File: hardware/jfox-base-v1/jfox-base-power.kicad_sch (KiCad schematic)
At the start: 13 parts, among them J50 PWR 1 RH, J51 PWR 2 LH

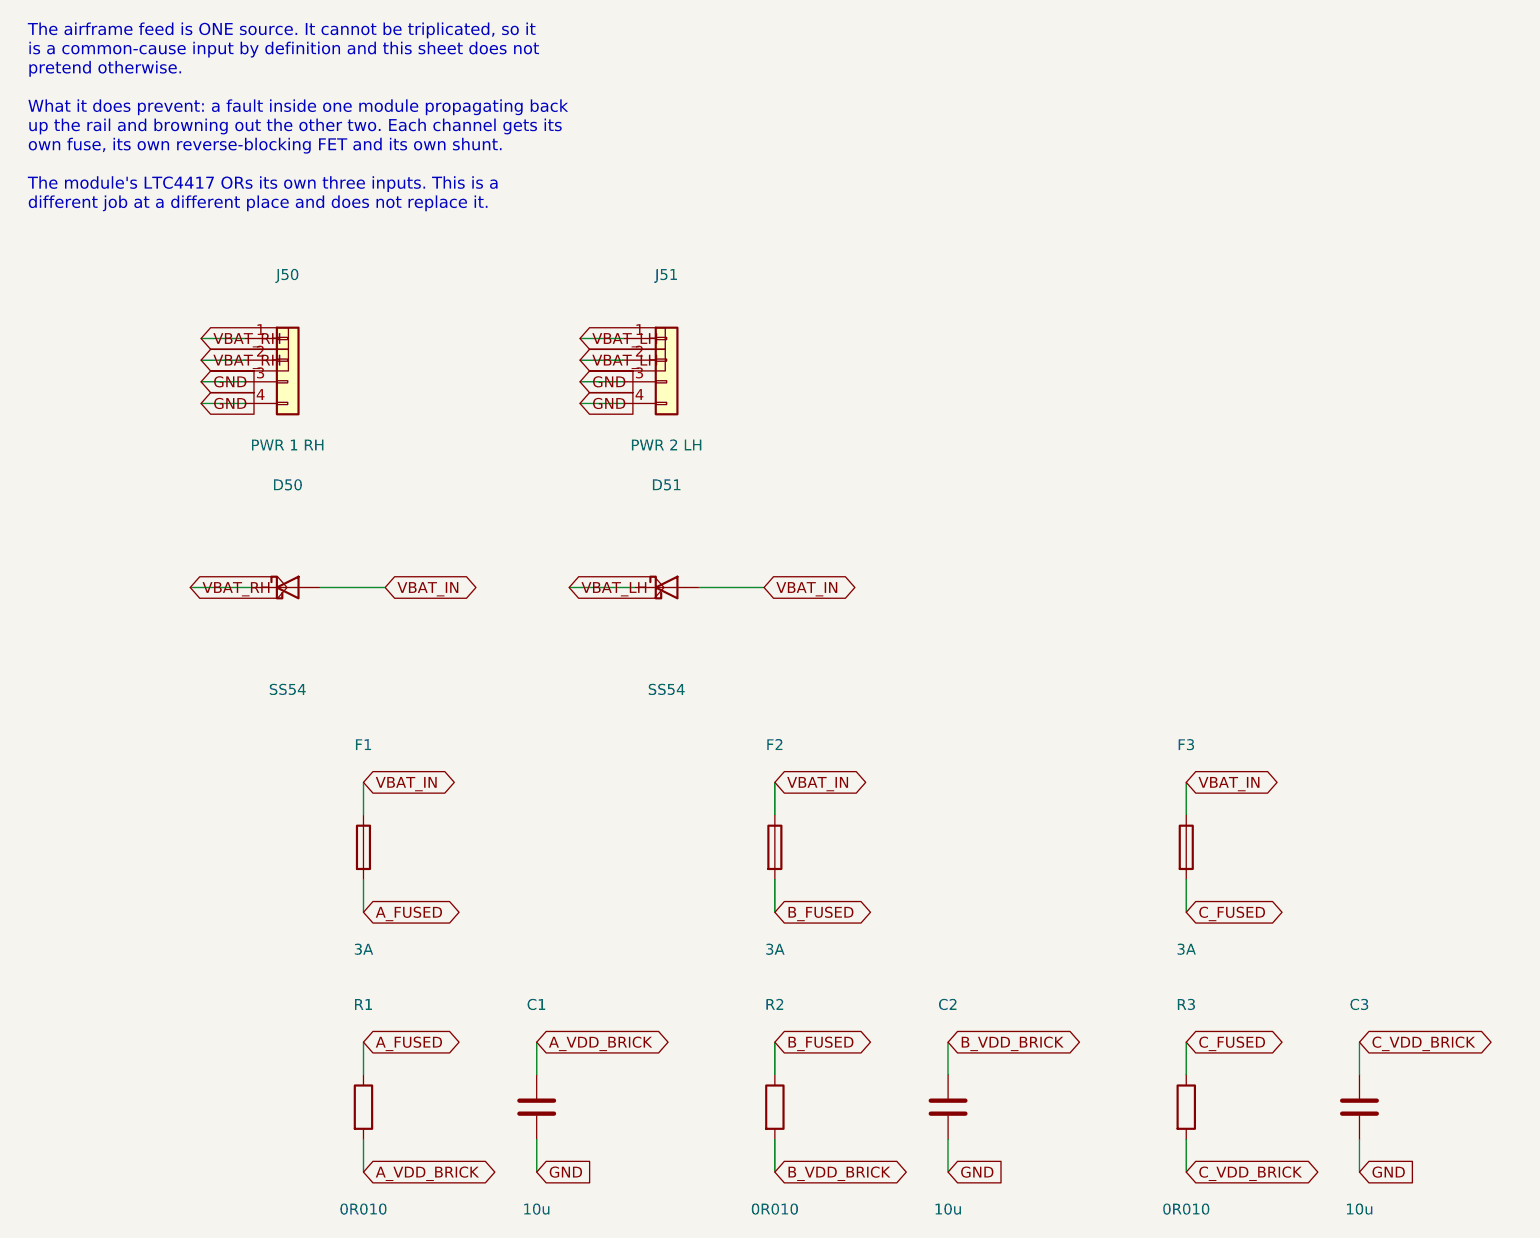
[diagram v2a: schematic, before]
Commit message: Provability: check the backplane, and fix the four defects that found
Nothing read JFOX-BASE-v1. Every checker in hardware/tools/ opened
jfox-fmu-v1/jfox-fmu.kicad_sch and only that, so no claim about the
backplane was provable - including the ones the requirements table recorded
as verified.

check_base_schematic.py now reads it: fused rails must reach a card socket,
the LTC4417 divider must produce the window it claims, that window must fit
every part downstream, and the feed-health outputs must reach a card AND be
driven. It failed on first run, which is the only reason to trust it.

What it found, in the order it found them:

  1. THE CARDS HAD NO POWER. The fuses put out A/B/C_FUSED and the card edge
     reads +5V_CARRIER. Both boards generated cleanly, both passed DRC, and
     the two halves were never connected to each other. The chain now
     terminates on the card rail past the shunt, not before it.

  2. THE FEEDS ARE NOT BATTERIES. VBAT_RH/VBAT_LH carry 5 V - the thresholds
     said so and the connectors are labelled PWR. Renamed PWR1_IN/PWR2_IN,
     output PWR_ORED. The name was the thing that was wrong.

  3. THE WINDOW PASSED MORE THAN A PART SURVIVES, and the binding part was
     not the one found by hand. The analysis flagged the AP2112K at 6.0 V
     against a 5.81 V threshold - 190 mV. The checker compared against every
     downstream part and found the ISOW1044 at 5.5 V: NEGATIVE 310 mV. A
     feed the controller reported as good would have destroyed the isolator.

     787k / 28k7 / 196k -> UV 4.50 V, OV 5.16 V
       ISOW1044  +338 mV      AP2112K  +838 mV

  4. THE ORING CONTROLLER'S OUTPUT WAS NEVER CONNECTED. Its pin map was
     written from the datasheet's block diagram, not the symbol: the pins
     are ~{VALID1..3} with overbars, VOUT not OUT, HYS not HYST, and there
     is no STAT pin at all. nets.get() returns None for an unknown key, so
     six pins were silently left unwired - VOUT among them. PWR_ORED was fed
     only by D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
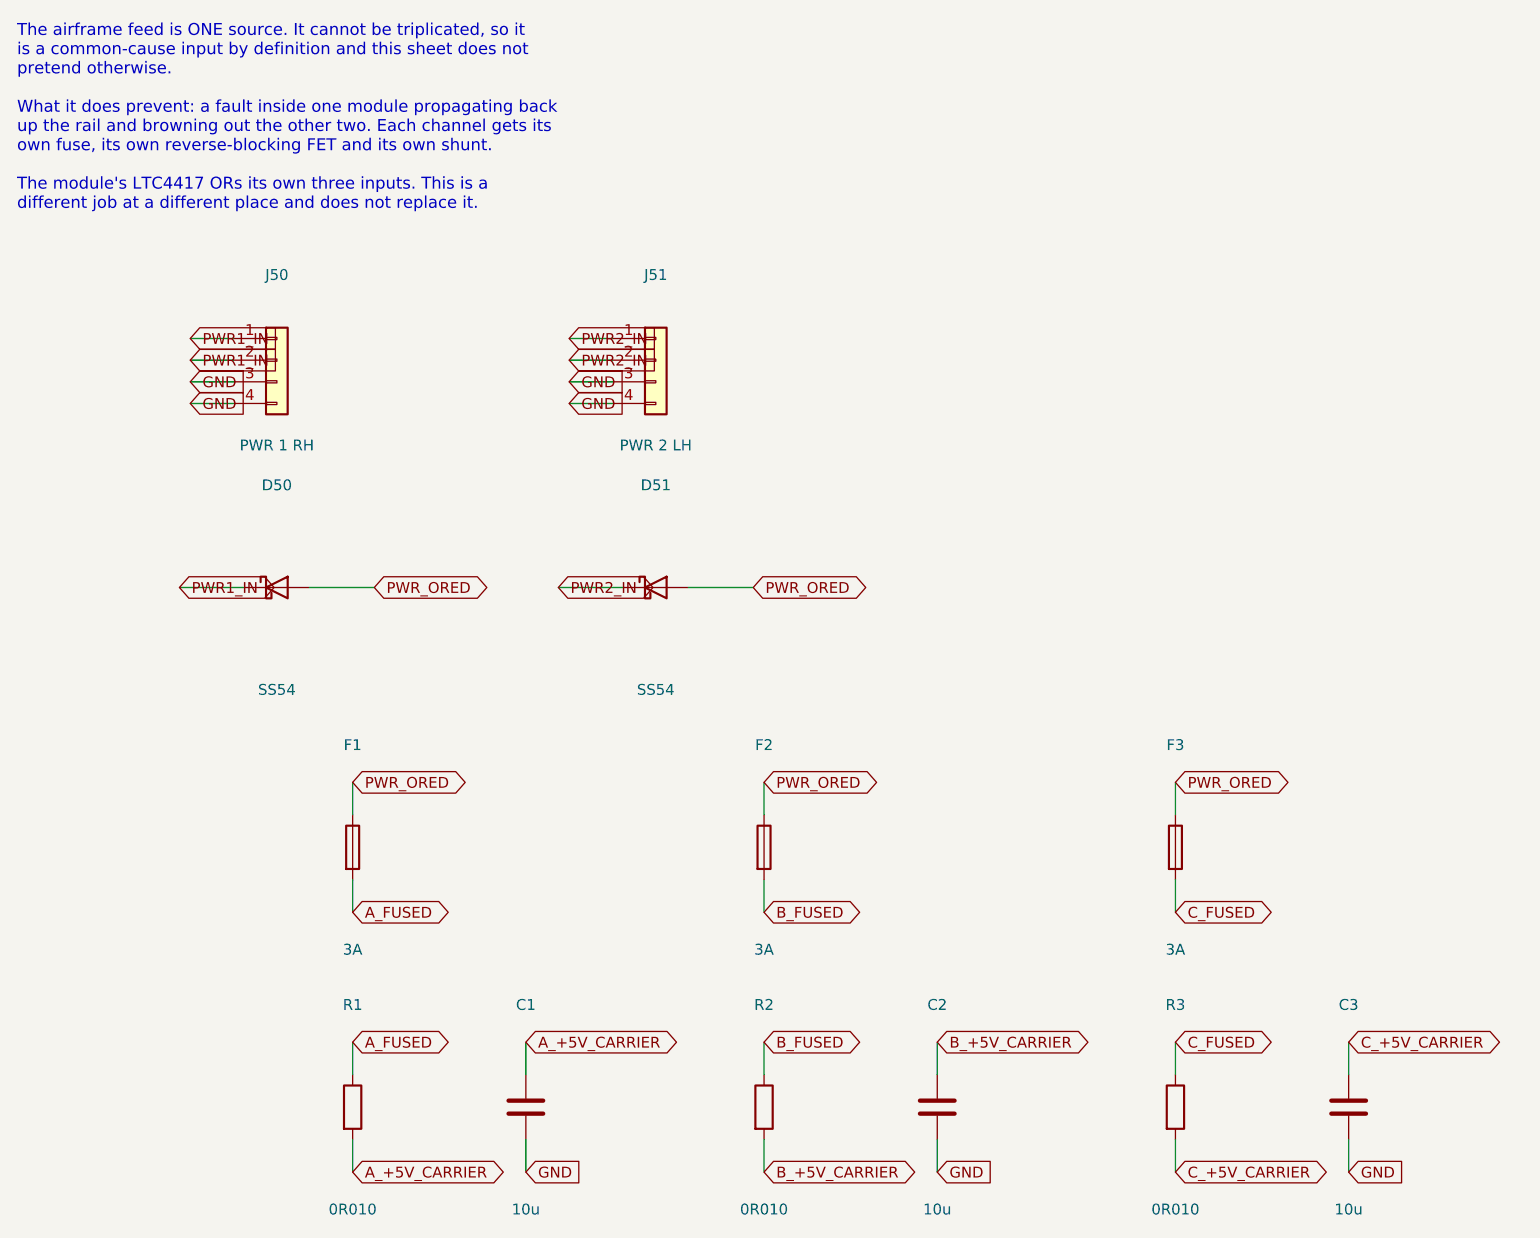
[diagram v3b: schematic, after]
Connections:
- net A_VDD_BRICK renamed A_+5V_CARRIER
- net B_VDD_BRICK renamed B_+5V_CARRIER
- net C_VDD_BRICK renamed C_+5V_CARRIER
- net VBAT_IN renamed PWR_ORED
- net VBAT_LH renamed PWR2_IN
- net VBAT_RH renamed PWR1_IN
